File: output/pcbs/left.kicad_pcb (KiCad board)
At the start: 2 copper layers, 123.1 x 95.2 mm, 40 parts

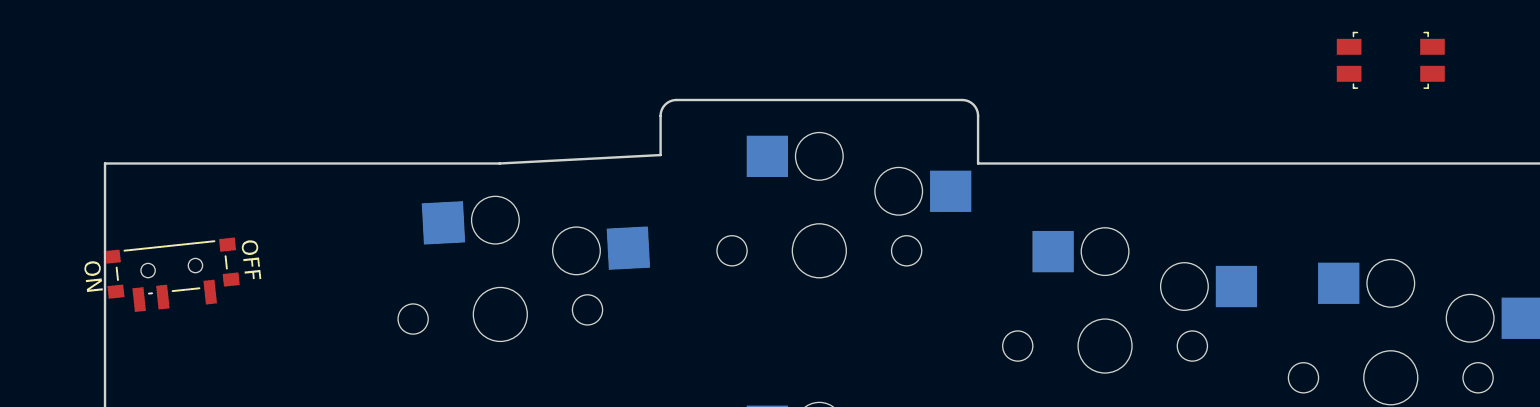
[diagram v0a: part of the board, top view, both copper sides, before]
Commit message: Try to line up power/reset switches with their outlines
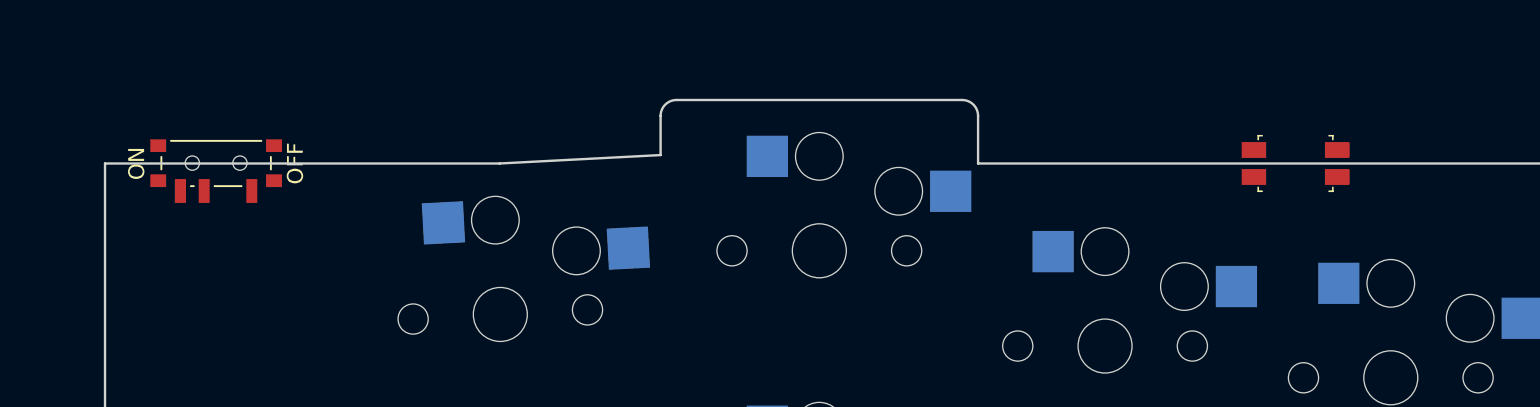
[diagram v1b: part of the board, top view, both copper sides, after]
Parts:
- moved RST1 8.85 mm to (65.1, -60.3)
- moved PWR1 7.18 mm to (-2.85, -60.3), turned to 90 degrees
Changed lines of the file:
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@@
   (footprint "ceoloide:reset_switch_smd_side"
     (layer "F.Cu")
-    (at 71.1483666 -66.8157089 0)
+    (at 65.1483667 -60.315708799999996 0)
     (property "Reference" "RST1"
       (at 0 0 0)
@@
   (footprint "ceoloide:power_switch_smd_side"
     (layer "F.Cu")
-    (at -5.6445371 -53.7041823 96)
+    (at -2.851633300000003 -60.315708799999996 90)
     (property "Reference" "PWR1"
-      (at -3.6 0 6)
+      (at -3.6 0 0)
       (layer "F.SilkS")
       hide
@@
     (fp_line (start 2.645 1.4) (end 2.845 1.2) (layer "F.Fab") (stroke (width 0.1) (type solid)))
     (fp_line (start 1.345 1.4) (end 2.645 1.4) (layer "F.Fab") (stroke (width 0.1) (type solid)))
-    (pad "" smd rect (at 1.125 -3.65 186) (size 1 0.8) (layers "F.Cu" "F.Paste" "F.Mask"))
-    (pad "" smd rect (at -1.085 -3.65 186) (size 1 0.8) (layers "F.Cu" "F.Paste" "F.Mask"))
-    (pad "" smd rect (at -1.085 3.65 186) (size 1 0.8) (layers "F.Cu" "F.Paste" "F.Mask"))
-    (pad "" smd rect (at 1.125 3.65 186) (size 1 0.8) (layers "F.Cu" "F.Paste" "F.Mask"))
-    (pad "1" smd rect (at -1.735 2.25 186) (size 0.7 1.5) (layers "F.Cu" "F.Paste" "F.Mask") )
-    (pad "2" smd rect (at -1.735 -0.75 186) (size 0.7 1.5) (layers "F.Cu" "F.Paste" "F.Mask") (net 76 "RAW"))
-    (pad "3" smd rect (at -1.735 -2.25 186) (size 0.7 1.5) (layers "F.Cu" "F.Paste" "F.Mask") (net 124 "BAT_P"))
-    (fp_text user "ON" (at 0 -5 96) (layer "F.SilkS")
+    (pad "" smd rect (at 1.125 -3.65 180) (size 1 0.8) (layers "F.Cu" "F.Paste" "F.Mask"))
+    (pad "" smd rect (at -1.085 -3.65 180) (size 1 0.8) (layers "F.Cu" "F.Paste" "F.Mask"))
+    (pad "" smd rect (at -1.085 3.65 180) (size 1 0.8) (layers "F.Cu" "F.Paste" "F.Mask"))
+    (pad "" smd rect (at 1.125 3.65 180) (size 1 0.8) (layers "F.Cu" "F.Paste" "F.Mask"))
+    (pad "1" smd rect (at -1.735 2.25 180) (size 0.7 1.5) (layers "F.Cu" "F.Paste" "F.Mask") )
+    (pad "2" smd rect (at -1.735 -0.75 180) (size 0.7 1.5) (layers "F.Cu" "F.Paste" "F.Mask") (net 76 "RAW"))
+    (pad "3" smd rect (at -1.735 -2.25 180) (size 0.7 1.5) (layers "F.Cu" "F.Paste" "F.Mask") (net 124 "BAT_P"))
+    (fp_text user "ON" (at 0 -5 90) (layer "F.SilkS")
       (effects (font (size 1 1) (thickness 0.15)))
     )
-    (fp_text user "OFF" (at 0 5 96) (layer "F.SilkS")
+    (fp_text user "OFF" (at 0 5 90) (layer "F.SilkS")
       (effects (font (size 1 1) (thickness 0.15)))
     )
@@
     (fp_line (start 1.425 2.85) (end 1.425 -2.85) (layer "F.SilkS") (stroke (width 0.12) (type solid)))
     (fp_line (start -1.425 -1.4) (end -1.425 -1.6) (layer "F.SilkS") (stroke (width 0.12) (type solid)))
-    (pad "" np_thru_hole circle (at 0.025 -1.5 186) (size 0.9 0.9) (drill 0.9) (layers "*.Cu" "*.Mask"))
-    (pad "" np_thru_hole circle (at 0.025 1.5 186) (size 0.9 0.9) (drill 0.9) (layers "*.Cu" "*.Mask"))
+    (pad "" np_thru_hole circle (at 0.025 -1.5 180) (size 0.9 0.9) (drill 0.9) (layers "*.Cu" "*.Mask"))
+    (pad "" np_thru_hole circle (at 0.025 1.5 180) (size 0.9 0.9) (drill 0.9) (layers "*.Cu" "*.Mask"))
   )
     (footprint "ceoloide:battery_connector_jst_ph_2"

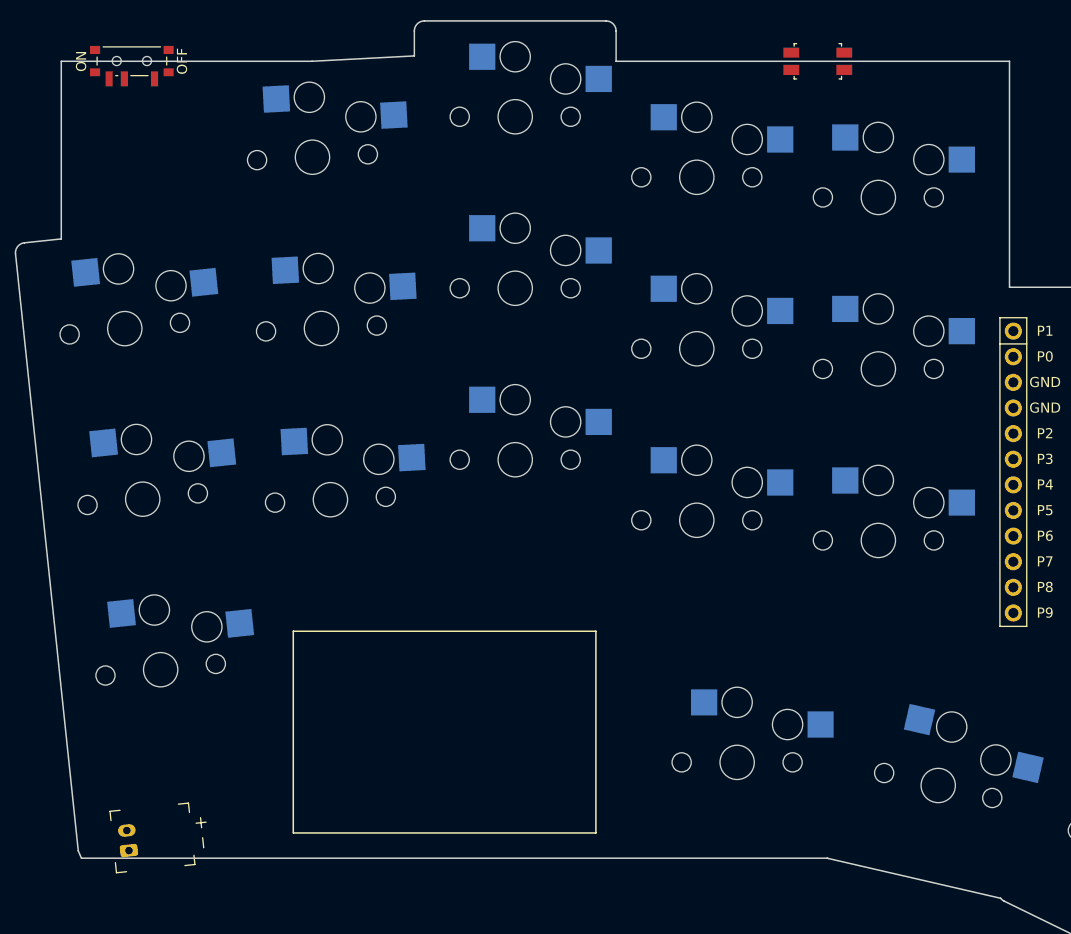
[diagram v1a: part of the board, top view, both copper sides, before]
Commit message: Reposition little components
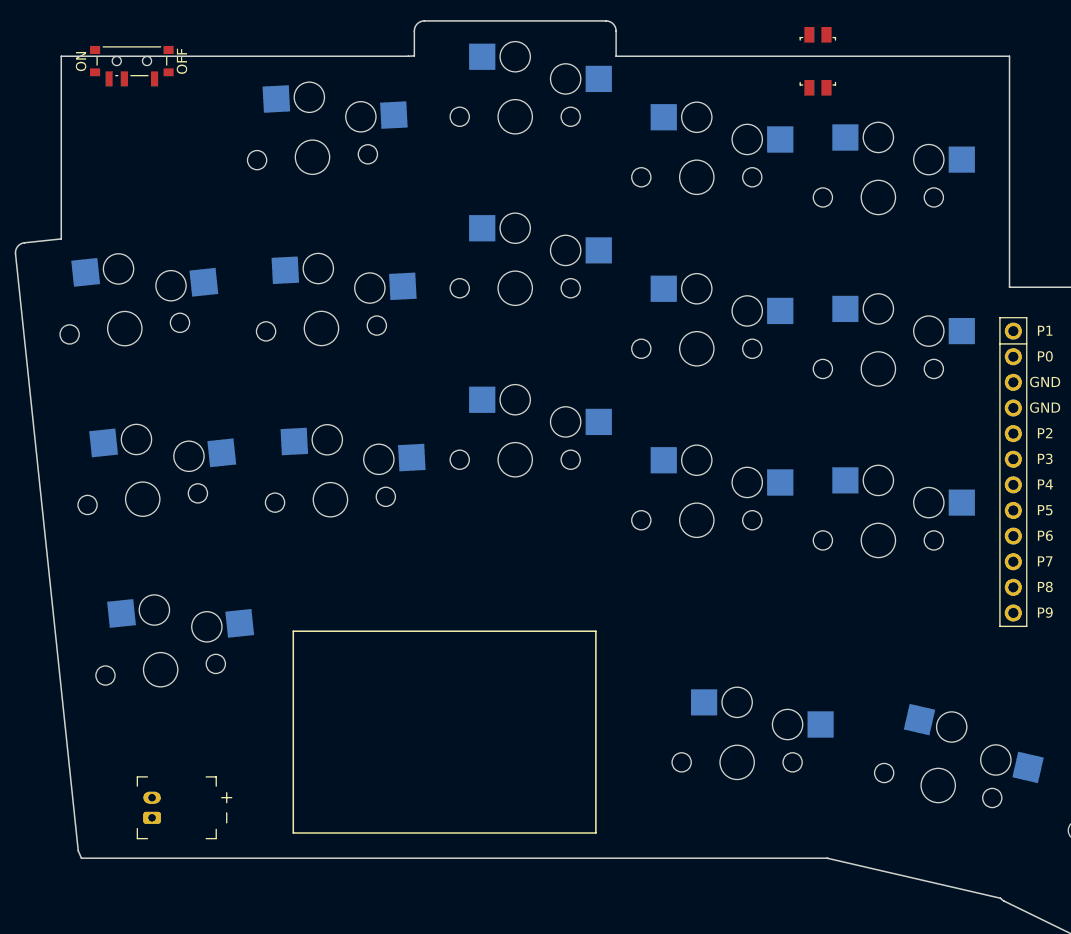
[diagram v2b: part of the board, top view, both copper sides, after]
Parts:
- moved JST1 4.04 mm to (-0.85, 13.7), turned to 90 degrees
- turned RST1 to 90 degrees
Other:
- outline, holes or cut-outs redrawn
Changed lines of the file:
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@@
   (footprint "ceoloide:reset_switch_smd_side"
     (layer "F.Cu")
-    (at 65.1483667 -60.315708799999996 0)
+    (at 65.1483667 -60.315708799999996 90)
     (property "Reference" "RST1"
-      (at 0 0 0)
+      (at 0 0 90)
       (layer "F.SilkS")
       hide
@@
     (fp_line (start 1.3 -2.75) (end 1.3 -1.75) (stroke (width 0.1) (type solid)) (layer "Dwgs.User"))
     (fp_line (start 2.35 -1.75) (end 2.35 1.75) (stroke (width 0.1) (type solid)) (layer "Dwgs.User"))
-    (pad "1" smd rect (at 2.625 -0.85 180) (size 1.55 1) (layers "F.Cu" "F.Paste" "F.Mask") (net 3 "GND"))
-    (pad "2" smd rect (at 2.625 0.85 180) (size 1.55 1) (layers "F.Cu" "F.Paste" "F.Mask") (net 77 "RST"))
-    (pad "3" smd rect (at -2.625 -0.85 180) (size 1.55 1) (layers "F.Cu" "F.Paste" "F.Mask") (net 3 "GND"))
-    (pad "4" smd rect (at -2.625 0.85 180) (size 1.55 1) (layers "F.Cu" "F.Paste" "F.Mask") (net 77 "RST"))
+    (pad "1" smd rect (at 2.625 -0.85 270) (size 1.55 1) (layers "F.Cu" "F.Paste" "F.Mask") (net 3 "GND"))
+    (pad "2" smd rect (at 2.625 0.85 270) (size 1.55 1) (layers "F.Cu" "F.Paste" "F.Mask") (net 77 "RST"))
+    (pad "3" smd rect (at -2.625 -0.85 270) (size 1.55 1) (layers "F.Cu" "F.Paste" "F.Mask") (net 3 "GND"))
+    (pad "4" smd rect (at -2.625 0.85 270) (size 1.55 1) (layers "F.Cu" "F.Paste" "F.Mask") (net 77 "RST"))
     (fp_line (start -2.35 -1.5) (end -2.35 -1.75) (stroke (width 0.1) (type solid)) (layer "F.SilkS"))
     (fp_line (start -2.35 1.5) (end -2.35 1.75) (stroke (width 0.1) (type solid)) (layer "F.SilkS"))
@@
     (footprint "ceoloide:battery_connector_jst_ph_2"
         (layer "F.Cu")
-        (at -3.2478898 16.9322536 96)
+        (at -0.8516334000000043 13.6842912 90)
         (property "Reference" "JST1"
-            (at 0 4.8 96)
+            (at 0 4.8 90)
             (layer "F.SilkS")
             hide
@@
         (fp_line (start 2.14 6.36) (end 3.06 6.36) (stroke (width 0.12) (type solid)) (layer "F.SilkS"))
         (fp_line (start 3.06 6.36) (end 3.06 5.36) (stroke (width 0.12) (type solid)) (layer "F.SilkS"))
-        (pad "1" thru_hole roundrect (at -1 0 96) (size 1.2 1.75) (drill 0.75) (layers "*.Cu" "*.Mask") (roundrect_rratio 0.20) (net 3 "GND"))
-        (pad "2" thru_hole oval (at 1 0 96) (size 1.2 1.75) (drill 0.75) (layers "*.Cu" "*.Mask") (net 124 "BAT_P"))
+        (pad "1" thru_hole roundrect (at -1 0 90) (size 1.2 1.75) (drill 0.75) (layers "*.Cu" "*.Mask") (roundrect_rratio 0.20) (net 3 "GND"))
+        (pad "2" thru_hole oval (at 1 0 90) (size 1.2 1.75) (drill 0.75) (layers "*.Cu" "*.Mask") (net 124 "BAT_P"))
     )
-  (gr_line (start 45.148366599999996 -60.315708799999996) (end 45.1483667 -63.315708799999996) (layer Edge.Cuts) (stroke (width 0.15) (type default)))
+  (gr_line (start 45.148366599999996 -60.815708799999996) (end 45.1483667 -63.315708799999996) (layer Edge.Cuts) (stroke (width 0.15) (type default)))
 (gr_arc (start 45.1483667 -63.315708799999996) (mid 44.855473499999995 -64.0228156) (end 44.1483667 -64.3157088) (layer Edge.Cuts) (stroke (width 0.15) (type default)))
 (gr_line (start 44.1483667 -64.3157088) (end 26.148366699999997 -64.3157088) (layer Edge.Cuts) (stroke (width 0.15) (type default)))
 (gr_arc (start 26.148366699999997 -64.3157088) (mid 25.4412599 -64.0228156) (end 25.148366699999997 -63.315708799999996) (layer Edge.Cuts) (stroke (width 0.15) (type default)))
 (gr_line (start 25.148366699999997 -63.315708799999996) (end 25.148366699999997 -60.84721104908856) (layer Edge.Cuts) (stroke (width 0.15) (type default)))
-(gr_line (start 15.006699386396312 -60.315708799999996) (end 25.148366699999997 -60.84721104908856) (layer Edge.Cuts) (stroke (width 0.15) (type default)))
 (gr_line (start -9.851633300000003 -42.7041617200161) (end -13.497685300000002 -42.320946199999995) (layer Edge.Cuts) (stroke (width 0.15) (type default)))
 (gr_arc (start -13.497685300000002 -42.3209462) (mid -14.170302800000002 -41.9557447) (end -14.387678700000002 -41.2218958) (layer Edge.Cuts) (stroke (width 0.15) (type default)))
@@
 (gr_arc (start 108.582185 15.089205999999997) (mid 108.6289095 14.325266699999998) (end 108.1217621 13.752040899999997) (layer Edge.Cuts) (stroke (width 0.15) (type default)))
 (gr_line (start 108.1213601 13.751844899999998) (end 102.4483666 10.984941108545385) (layer Edge.Cuts) (stroke (width 0.15) (type default)))
+(gr_line (start 24.54726792343898 -60.815708799999996) (end 25.148366699999997 -60.84721104908856) (layer Edge.Cuts) (stroke (width 0.15) (type default)))
 (gr_line (start 84.1483666 -37.9157089) (end 102.4483666 -37.9157089) (layer Edge.Cuts) (stroke (width 0.15) (type default)))
 (gr_line (start 102.4483666 10.984941108545385) (end 102.4483666 -37.9157089) (layer Edge.Cuts) (stroke (width 0.15) (type default)))
 (gr_line (start -7.851633400000004 18.6842912) (end -8.1682351 17.9521569) (layer Edge.Cuts) (stroke (width 0.15) (type default)))
-(gr_line (start -9.851633300000003 -42.7041617200161) (end -9.851633300000003 -60.315708799999996) (layer Edge.Cuts) (stroke (width 0.15) (type default)))
-(gr_line (start -9.851633300000003 -60.315708799999996) (end 15.006699386396312 -60.315708799999996) (layer Edge.Cuts) (stroke (width 0.15) (type default)))
-(gr_line (start 45.148366599999996 -60.315708799999996) (end 84.1483667 -60.315708799999996) (layer Edge.Cuts) (stroke (width 0.15) (type default)))
-(gr_line (start 84.1483667 -60.315708799999996) (end 84.1483666 -37.9157089) (layer Edge.Cuts) (stroke (width 0.15) (type default)))
+(gr_line (start -9.851633300000003 -42.7041617200161) (end -9.851633300000003 -60.815708799999996) (layer Edge.Cuts) (stroke (width 0.15) (type default)))
+(gr_line (start -9.851633300000003 -60.815708799999996) (end 24.54726792343898 -60.815708799999996) (layer Edge.Cuts) (stroke (width 0.15) (type default)))
+(gr_line (start 45.148366599999996 -60.815708799999996) (end 84.1483667 -60.815708799999996) (layer Edge.Cuts) (stroke (width 0.15) (type default)))
+(gr_line (start 84.1483667 -60.815708799999996) (end 84.1483666 -37.9157089) (layer Edge.Cuts) (stroke (width 0.15) (type default)))
 (gr_line (start 13.148366599999996 -3.8157087999999995) (end 13.148366599999996 16.1842912) (layer F.SilkS) (stroke (width 0.15) (type default)))
 (gr_line (start 13.148366599999996 16.1842912) (end 43.148366599999996 16.1842912) (layer F.SilkS) (stroke (width 0.15) (type default)))
